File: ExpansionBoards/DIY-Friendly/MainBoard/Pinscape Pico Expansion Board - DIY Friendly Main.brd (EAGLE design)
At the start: 160 x 107 mm, 116 parts, among them IC1 UCC27524P, IC10 ULN2803A, IC11 SN74HC74NE4, IC12 S-80833CLY, IC13 PC827, IC14 SN74HC165N, IC15 SN74HC165N, IC16 SN74HC165N, IC17 SN74HC165N, IC2 UCC27524P, IC3 UCC27524P, IC4 UCC27524P, IC5 UCC27524P, IC6 UCC27524P, IC7 ULN2803A, IC8 ULN2803A, IC9 ULN2803A, J1 30316-6002HBROTATED, J10 215079-4, J11 640454-2, J13 640445-2, J14 SSQ-108-02-T-S-RA, J2 640445-6, J3 640445-5, J4 640445-9, J5 1-640456-0, J6 1-640456-0, J7 1-640456-0, J8 1-640456-0, J9 30308-6002HB, Q1 STP19NF20, Q10 STP19NF20, Q11 STP19NF20, Q12 STP19NF20, Q13 BC337-25, Q15 2N5195G, Q16 2N2222A, Q2 FDPF085N10A, Q3 STP19NF20, Q4 STP19NF20, Q5 STP19NF20, Q6 STP19NF20, Q7 STP19NF20, Q8 STP19NF20, Q9 STP19NF20

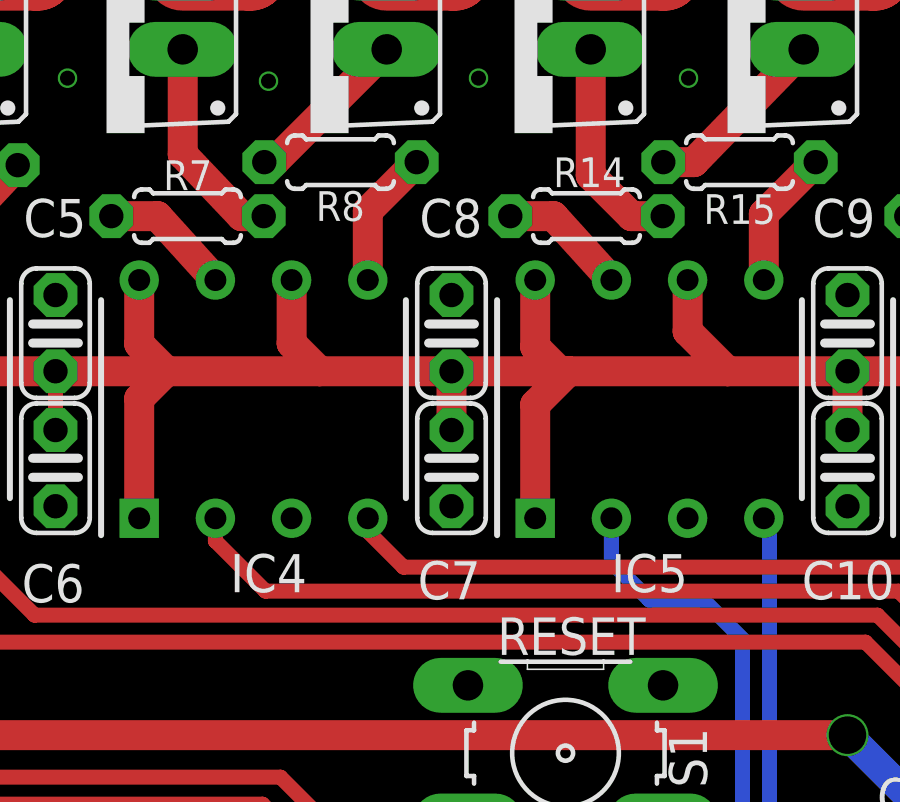
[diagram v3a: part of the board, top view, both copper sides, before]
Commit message: exp boards: DIY-friendly main: add button header pin labels; add button header pin label diagram to readme
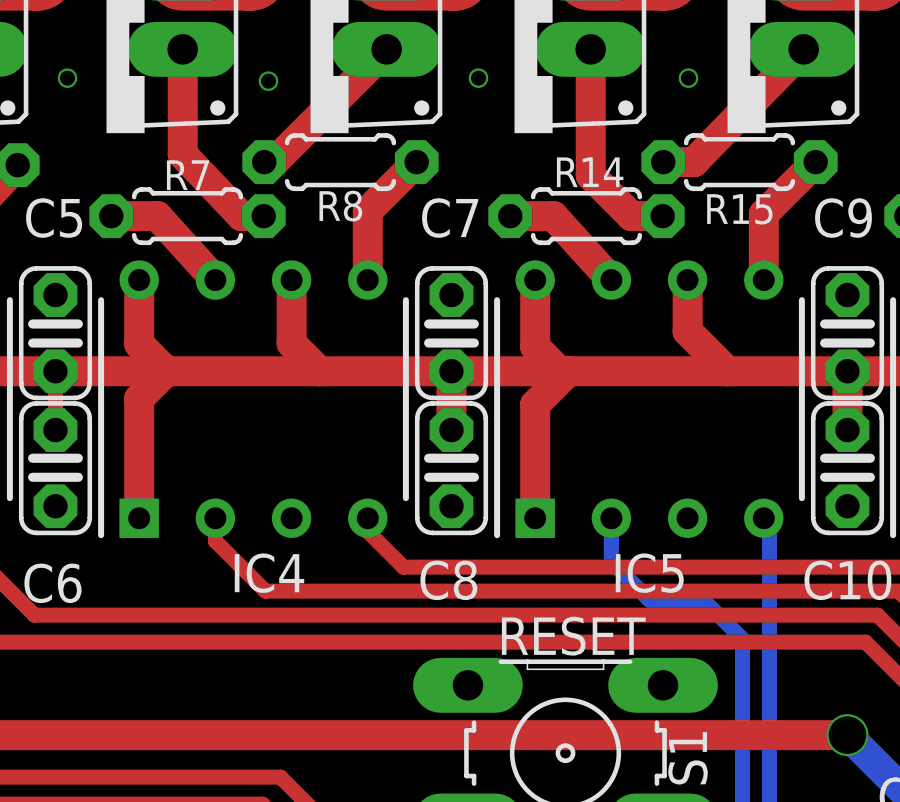
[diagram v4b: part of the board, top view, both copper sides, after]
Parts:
- C7: value 4.7uF -> 100nF
- C8: value 100nF -> 4.7uF
- moved C7 4.50 mm to (80.9, 71.3), turned to 270 degrees
- moved C8 4.50 mm to (80.9, 66.8), turned to 90 degrees
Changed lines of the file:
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@@
 <grid distance="0.1" unitdist="mm" unit="mm" style="lines" multiple="1" display="yes" altdistance="0.025" altunitdist="inch" altunit="inch"/>
 <layers>
-<layer number="1" name="Top" color="4" fill="1" visible="no" active="yes"/>
+<layer number="1" name="Top" color="4" fill="1" visible="yes" active="yes"/>
 <layer number="2" name="Route2" color="1" fill="3" visible="no" active="no"/>
 <layer number="3" name="Route3" color="4" fill="3" visible="no" active="no"/>
 <layer number="14" name="Route14" color="1" fill="6" visible="no" active="no"/>
 <layer number="15" name="Route15" color="4" fill="6" visible="no" active="no"/>
-<layer number="16" name="Bottom" color="1" fill="1" visible="no" active="yes"/>
+<layer number="16" name="Bottom" color="1" fill="1" visible="yes" active="yes"/>
 <layer number="17" name="Pads" color="2" fill="1" visible="yes" active="yes"/>
 <layer number="18" name="Vias" color="2" fill="1" visible="yes" active="yes"/>
-<layer number="19" name="Unrouted" color="6" fill="1" visible="no" active="yes"/>
+<layer number="19" name="Unrouted" color="6" fill="1" visible="yes" active="yes"/>
 <layer number="20" name="Dimension" color="15" fill="1" visible="yes" active="yes"/>
 <layer number="21" name="tPlace" color="7" fill="1" visible="yes" active="yes"/>
-<layer number="22" name="bPlace" color="7" fill="1" visible="no" active="yes"/>
+<layer number="22" name="bPlace" color="7" fill="1" visible="yes" active="yes"/>
 <layer number="23" name="tOrigins" color="15" fill="1" visible="yes" active="yes"/>
-<layer number="24" name="bOrigins" color="15" fill="1" visible="no" active="yes"/>
+<layer number="24" name="bOrigins" color="15" fill="1" visible="yes" active="yes"/>
 <layer number="25" name="tNames" color="7" fill="1" visible="yes" active="yes"/>
-<layer number="26" name="bNames" color="7" fill="1" visible="no" active="yes"/>
+<layer number="26" name="bNames" color="7" fill="1" visible="yes" active="yes"/>
 <layer number="27" name="tValues" color="7" fill="1" visible="yes" active="yes"/>
-<layer number="28" name="bValues" color="7" fill="1" visible="no" active="yes"/>
-<layer number="29" name="tStop" color="7" fill="3" visible="yes" active="yes"/>
+<layer number="28" name="bValues" color="7" fill="1" visible="yes" active="yes"/>
+<layer number="29" name="tStop" color="7" fill="3" visible="no" active="yes"/>
 <layer number="30" name="bStop" color="7" fill="6" visible="no" active="yes"/>
 <layer number="31" name="tCream" color="7" fill="4" visible="no" active="yes"/>
@@
 <layer number="37" name="tTest" color="7" fill="1" visible="no" active="yes"/>
 <layer number="38" name="bTest" color="7" fill="1" visible="no" active="yes"/>
-<layer number="39" name="tKeepout" color="4" fill="11" visible="no" active="yes"/>
-<layer number="40" name="bKeepout" color="1" fill="11" visible="no" active="yes"/>
-<layer number="41" name="tRestrict" color="4" fill="10" visible="no" active="yes"/>
-<layer number="42" name="bRestrict" color="1" fill="10" visible="no" active="yes"/>
-<layer number="43" name="vRestrict" color="2" fill="10" visible="no" active="yes"/>
+<layer number="39" name="tKeepout" color="4" fill="11" visible="yes" active="yes"/>
+<layer number="40" name="bKeepout" color="1" fill="11" visible="yes" active="yes"/>
+<layer number="41" name="tRestrict" color="4" fill="10" visible="yes" active="yes"/>
+<layer number="42" name="bRestrict" color="1" fill="10" visible="yes" active="yes"/>
+<layer number="43" name="vRestrict" color="2" fill="10" visible="yes" active="yes"/>
 <layer number="44" name="Drills" color="7" fill="1" visible="no" active="yes"/>
 <layer number="45" name="Holes" color="7" fill="1" visible="no" active="yes"/>
 <layer number="46" name="Milling" color="3" fill="1" visible="no" active="yes"/>
 <layer number="47" name="Measures" color="7" fill="1" visible="no" active="yes"/>
-<layer number="48" name="Document" color="7" fill="1" visible="no" active="yes"/>
-<layer number="49" name="Reference" color="7" fill="1" visible="no" active="yes"/>
+<layer number="48" name="Document" color="7" fill="1" visible="yes" active="yes"/>
+<layer number="49" name="Reference" color="7" fill="1" visible="yes" active="yes"/>
 <layer number="50" name="dxf" color="7" fill="1" visible="no" active="no"/>
-<layer number="51" name="tDocu" color="7" fill="1" visible="no" active="yes"/>
-<layer number="52" name="bDocu" color="7" fill="1" visible="no" active="yes"/>
+<layer number="51" name="tDocu" color="7" fill="1" visible="yes" active="yes"/>
+<layer number="52" name="bDocu" color="7" fill="1" visible="yes" active="yes"/>
 <layer number="53" name="tPadExt" color="7" fill="1" visible="no" active="no"/>
 <layer number="54" name="bPadExt" color="1" fill="1" visible="no" active="no"/>
@@
 <layer number="60" name="bCarbon" color="7" fill="1" visible="no" active="no"/>
 <layer number="61" name="stand" color="7" fill="1" visible="no" active="no"/>
-<layer number="88" name="SimResults" color="9" fill="1" visible="no" active="yes"/>
-<layer number="89" name="SimProbes" color="9" fill="1" visible="no" active="yes"/>
+<layer number="88" name="SimResults" color="9" fill="1" visible="yes" active="yes"/>
+<layer number="89" name="SimProbes" color="9" fill="1" visible="yes" active="yes"/>
 <layer number="90" name="Modules" color="5" fill="1" visible="no" active="no"/>
 <layer number="91" name="Nets" color="2" fill="1" visible="no" active="no"/>
@@
 <layer number="98" name="Guide" color="6" fill="1" visible="no" active="no"/>
 <layer number="99" name="SpiceOrder" color="5" fill="1" visible="no" active="no"/>
-<layer number="100" name="US-Transistor" color="7" fill="1" visible="no" active="yes"/>
-<layer number="101" name="EU-Transistor" color="7" fill="1" visible="no" active="yes"/>
+<layer number="100" name="US-Transistor" color="7" fill="1" visible="yes" active="yes"/>
+<layer number="101" name="EU-Transistor" color="7" fill="1" visible="yes" active="yes"/>
 <layer number="102" name="Vscore" color="7" fill="1" visible="no" active="yes"/>
 <layer number="103" name="fp3" color="7" fill="1" visible="no" active="yes"/>
@@
 <attribute name="VALUE" x="78.4336" y="77.5114" size="0.9906" layer="27" ratio="10" rot="R180"/>
 </element>
-<element name="C8" library="rcl" package="C025-024X044" value="100nF" x="80.9" y="71.3" smashed="yes" rot="R270">
+<element name="C7" library="rcl" package="C025-024X044" value="100nF" x="80.9" y="71.3" smashed="yes" rot="R270">
 <attribute name="PARTNO" value="K104K15X7RF5TL2" x="-38" y="71.3" size="0.6" layer="27" rot="R270" display="off"/>
 <attribute name="NAME" x="80.878" y="74.503" size="1.27" layer="25" ratio="10" rot="R180" align="top-center"/>
 <attribute name="VALUE" x="80.878" y="73.667" size="0.6" layer="27" ratio="10" rot="R180" align="top-center"/>
 </element>
-<element name="C7" library="rcl" package="C025-024X044" value="4.7uF" x="80.9" y="66.8" smashed="yes" rot="R90">
+<element name="C8" library="rcl" package="C025-024X044" value="4.7uF" x="80.9" y="66.8" smashed="yes" rot="R90">
 <attribute name="PARTNO" value="810-FG14X5R1H475KRT0" x="213.1" y="51" size="0.6" layer="27" rot="R90" display="off"/>
 <attribute name="NAME" x="80.822" y="63.697" size="1.27" layer="25" ratio="10" align="top-center"/>
@@
 <contactref element="Q6" pad="3"/>
 <contactref element="Q7" pad="3"/>
+<contactref element="C7" pad="1"/>
 <contactref element="C8" pad="1"/>
-<contactref element="C7" pad="1"/>
 <contactref element="Q8" pad="3"/>
 <via x="34.3" y="79.7" extent="1-16" drill="0.5"/>
@@
 <contactref element="IC4" pad="8"/>
 <contactref element="IC4" pad="1"/>
+<contactref element="C8" pad="2"/>
 <contactref element="C7" pad="2"/>
-<contactref element="C8" pad="2"/>
 <wire x1="54.5" y1="70.03" x2="58" y2="70.03" width="1" layer="1"/>
 <wire x1="58" y1="70.03" x2="58.4" y2="70.03" width="0.5" layer="1"/>

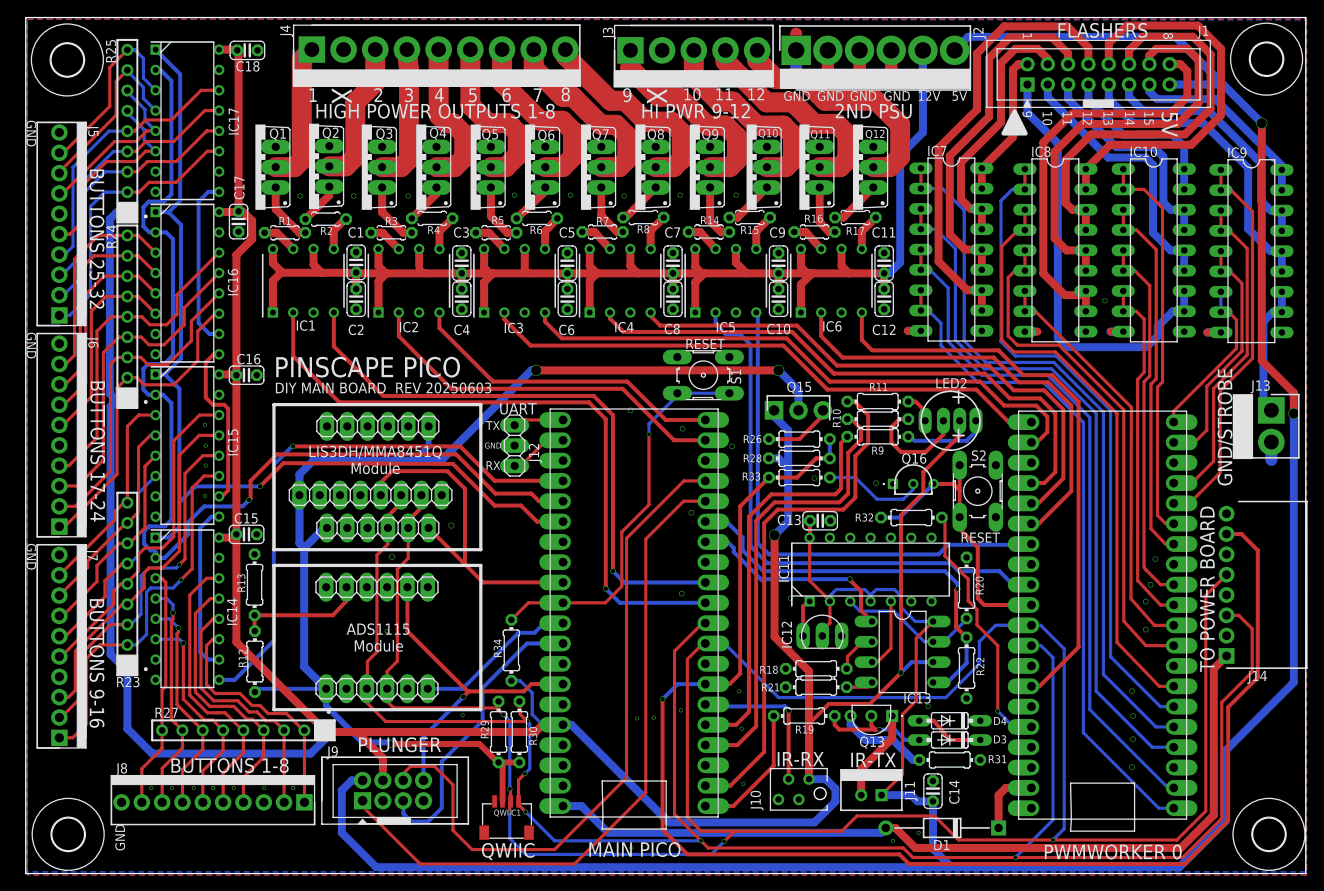
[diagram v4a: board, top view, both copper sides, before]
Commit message: Power Distro board BOM: add missing 24V/48V SMPS connectors (J18, J19)
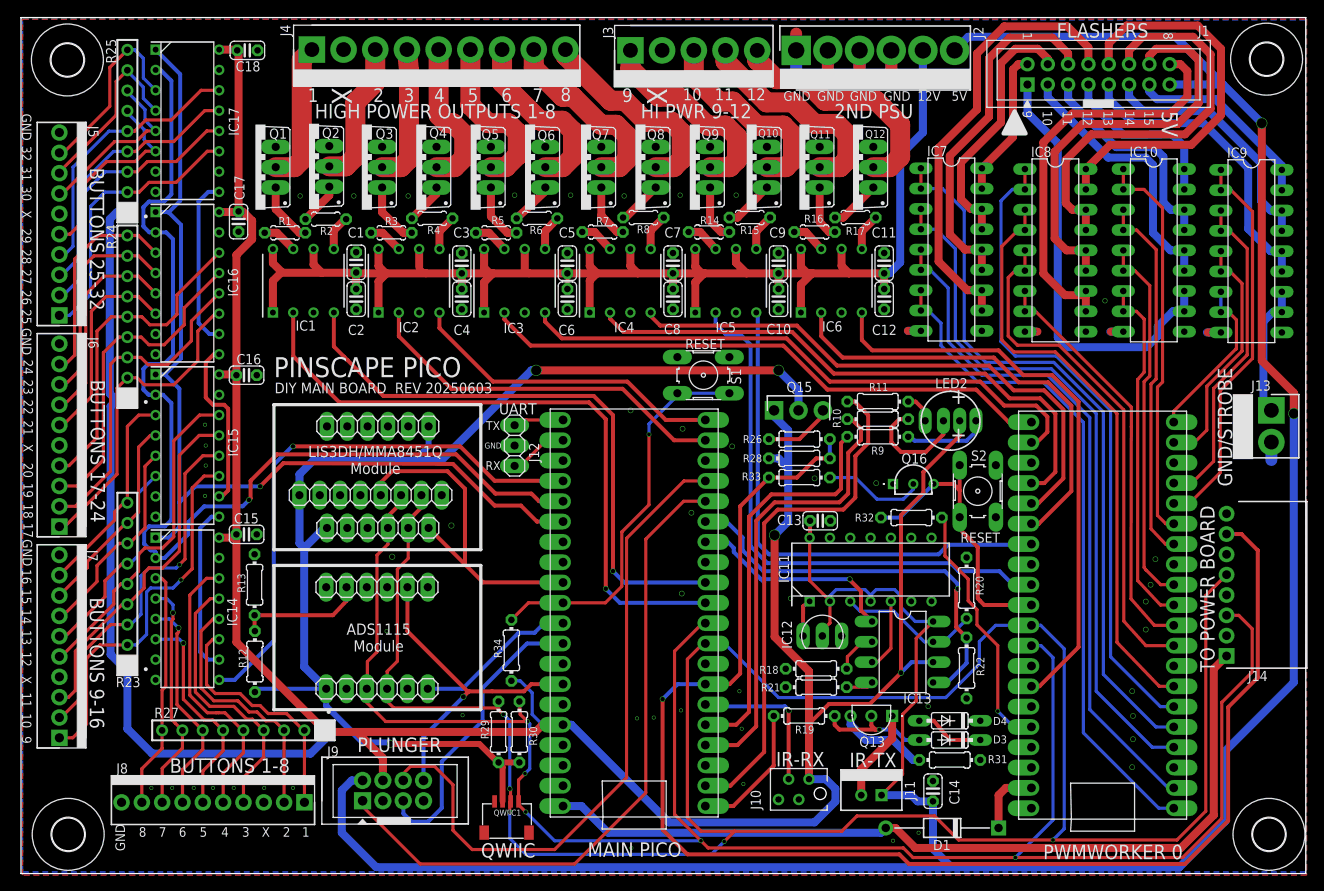
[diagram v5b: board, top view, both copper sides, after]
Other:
- board size 160 x 107 mm -> 160.6 x 107 mm
- board text added: "16"
- board text added: "17"
- board text added: "18"
- board text added: "19"
- board text added: "20"
- board text added: "21"
- board text added: "22"
- board text added: "23"
- board text added: "24"
- board text added: "25"
- board text added: "26"
- board text added: "27"
- board text added: "28"
- board text added: "29"
- board text added: "30"
- board text added: "31"
- board text added: "32"
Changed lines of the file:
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@@
 <board>
 <plain>
-<wire x1="0" y1="-5" x2="160" y2="-5" width="0" layer="20"/>
+<wire x1="-0.6" y1="-5" x2="160" y2="-5" width="0" layer="20"/>
 <wire x1="160" y1="-5" x2="160" y2="102" width="0" layer="20"/>
-<wire x1="160" y1="102" x2="0" y2="102" width="0" layer="20"/>
-<wire x1="0" y1="102" x2="0" y2="-5" width="0" layer="20"/>
+<wire x1="160" y1="102" x2="-0.6" y2="102" width="0" layer="20"/>
+<wire x1="-0.6" y1="102" x2="-0.6" y2="-5" width="0" layer="20"/>
 <text x="44.1" y="24.5" size="1.4" layer="21" ratio="15" align="center">ADS1115
 Module</text>
@@
 </polygon>
 <text x="11.8" y="-0.5" size="1.2" layer="25" ratio="15" rot="SR90" align="center">GND</text>
-<text x="0.7" y="34.6" size="1.2" layer="25" ratio="15" rot="SR270" align="center">GND</text>
-<text x="0.7" y="61" size="1.2" layer="25" ratio="15" rot="SR270" align="center">GND</text>
-<text x="0.7" y="87.5" size="1.2" layer="25" ratio="15" rot="SR270" align="center">GND</text>
+<text x="0.2" y="35.1" size="1.2" layer="25" ratio="15" rot="SR270" align="center">GND</text>
+<text x="0.1" y="61.5" size="1.2" layer="25" ratio="15" rot="SR270" align="center">GND</text>
+<text x="0.1" y="88.3" size="1.2" layer="25" ratio="15" rot="SR270" align="center">GND</text>
+<text x="35" y="0.2" size="1.2" layer="25" ratio="15" rot="SR0" align="center">1</text>
+<text x="32.6" y="0.2" size="1.2" layer="25" ratio="15" rot="SR0" align="center">2</text>
+<text x="30" y="0.2" size="1.2" layer="25" ratio="15" rot="SR0" align="center">X</text>
+<text x="27.5" y="0.2" size="1.2" layer="25" ratio="15" rot="SR0" align="center">3</text>
+<text x="24.9" y="0.2" size="1.2" layer="25" ratio="15" rot="SR0" align="center">4</text>
+<text x="22.2" y="0.2" size="1.2" layer="25" ratio="15" rot="SR0" align="center">5</text>
+<text x="19.6" y="0.2" size="1.2" layer="25" ratio="15" rot="SR0" align="center">6</text>
+<text x="17.1" y="0.2" size="1.2" layer="25" ratio="15" rot="SR0" align="center">7</text>
+<text x="14.6" y="0.2" size="1.2" layer="25" ratio="15" rot="SR0" align="center">8</text>
+<text x="0.1" y="11.7" size="1.2" layer="25" ratio="15" rot="SR270" align="center">9</text>
+<text x="0.1" y="14.1" size="1.2" layer="25" ratio="15" rot="SR270" align="center">10</text>
+<text x="0.1" y="16.7" size="1.2" layer="25" ratio="15" rot="SR270" align="center">11</text>
+<text x="0.1" y="19.2" size="1.2" layer="25" ratio="15" rot="SR270" align="center">X</text>
+<text x="0.1" y="21.8" size="1.2" layer="25" ratio="15" rot="SR270" align="center">12</text>
+<text x="0.1" y="24.5" size="1.2" layer="25" ratio="15" rot="SR270" align="center">13</text>
+<text x="0.1" y="27.1" size="1.2" layer="25" ratio="15" rot="SR270" align="center">14</text>
+<text x="0.1" y="29.6" size="1.2" layer="25" ratio="15" rot="SR270" align="center">15</text>
+<text x="0.1" y="32.1" size="1.2" layer="25" ratio="15" rot="SR270" align="center">16</text>
+<text x="0.3" y="37.9" size="1.2" layer="25" ratio="15" rot="SR270" align="center">17</text>
+<text x="0.3" y="40.3" size="1.2" layer="25" ratio="15" rot="SR270" align="center">18</text>
+<text x="0.3" y="42.9" size="1.2" layer="25" ratio="15" rot="SR270" align="center">19</text>
+<text x="0.3" y="45.4" size="1.2" layer="25" ratio="15" rot="SR270" align="center">20</text>
+<text x="0.3" y="48.2" size="1.2" layer="25" ratio="15" rot="SR270" align="center">X</text>
+<text x="0.3" y="50.7" size="1.2" layer="25" ratio="15" rot="SR270" align="center">21</text>
+<text x="0.3" y="53.3" size="1.2" layer="25" ratio="15" rot="SR270" align="center">22</text>
+<text x="0.3" y="55.8" size="1.2" layer="25" ratio="15" rot="SR270" align="center">23</text>
+<text x="0.3" y="58.3" size="1.2" layer="25" ratio="15" rot="SR270" align="center">24</text>
+<text x="0.1" y="64.6" size="1.2" layer="25" ratio="15" rot="SR270" align="center">25</text>
+<text x="0.1" y="67" size="1.2" layer="25" ratio="15" rot="SR270" align="center">26</text>
+<text x="0.1" y="69.6" size="1.2" layer="25" ratio="15" rot="SR270" align="center">27</text>
+<text x="0.1" y="72.1" size="1.2" layer="25" ratio="15" rot="SR270" align="center">28</text>
+<text x="0.1" y="74.7" size="1.2" layer="25" ratio="15" rot="SR270" align="center">29</text>
+<text x="0.1" y="77.4" size="1.2" layer="25" ratio="15" rot="SR270" align="center">X</text>
+<text x="0.1" y="80" size="1.2" layer="25" ratio="15" rot="SR270" align="center">30</text>
+<text x="0.1" y="82.5" size="1.2" layer="25" ratio="15" rot="SR270" align="center">31</text>
+<text x="0.1" y="85" size="1.2" layer="25" ratio="15" rot="SR270" align="center">32</text>
 </plain>
 <attributes>
@@
 <contactref element="PICO1" pad="GND@6"/>
 <polygon width="0.4064" layer="1">
-<vertex x="0.2" y="101.8"/>
+<vertex x="-0.4" y="101.8"/>
 <vertex x="160.1" y="101.8"/>
 <vertex x="160.1" y="-5.2"/>
-<vertex x="0.2" y="-5.2"/>
+<vertex x="-0.4" y="-5.2"/>
 </polygon>
 <polygon width="0.4064" layer="16">
-<vertex x="0.2" y="101.8"/>
+<vertex x="-0.4" y="101.8"/>
 <vertex x="160" y="101.7"/>
 <vertex x="160" y="-4.8"/>
-<vertex x="0.2" y="-4.8"/>
+<vertex x="-0.4" y="-4.8"/>
 </polygon>
 <contactref element="J8" pad="10"/>
